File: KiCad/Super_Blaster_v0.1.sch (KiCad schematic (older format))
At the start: 9 parts

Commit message: Started Connections
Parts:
- removed U? (x3): FT601Q, symbol FT601Q
- gave numbers to parts that had none: 1
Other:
- moved on the sheet: U2B, U2C, U2D, U2E
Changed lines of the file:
@@
 EESchema Schematic File Version 2
+LIBS:Super_Blaster_v0.1-rescue
 LIBS:power
 LIBS:device
@@
 LIBS:valves
 LIBS:Homebrew
+LIBS:Super_Blaster_v0.1-cache
 EELAYER 25 0
 EELAYER END
-$Descr A4 11693 8268
+$Descr USLetter 11000 8500
 encoding utf-8
-Sheet 1 1
+Sheet 1 2
 Title ""
 Date ""
@@
 $EndDescr
 $Comp
-L FT601Q U?
-U 1 1 58FB0266
-P 1950 2150
-F 0 "U?" H 1450 3100 60  0000 C CNN
-F 1 "FT601Q" H 1950 1250 60  0000 C CNN
-F 2 "" H 1750 2150 60  0001 C CNN
-F 3 "" H 1750 2150 60  0001 C CNN
-	1    1950 2150
-	1    0    0    -1
-$EndComp
-$Comp
-L FT601Q U?
-U 2 1 58FB02E0
-P 1600 4650
-F 0 "U?" H 1100 5600 60  0000 C CNN
-F 1 "FT601Q" H 1600 3750 60  0000 C CNN
-F 2 "" H 1400 4650 60  0001 C CNN
-F 3 "" H 1400 4650 60  0001 C CNN
-	2    1600 4650
-	1    0    0    -1
-$EndComp
-$Comp
-L FT601Q U?
-U 3 1 58FB0355
-P 1550 6700
-F 0 "U?" H 1050 7650 60  0000 C CNN
-F 1 "FT601Q" H 1550 5800 60  0000 C CNN
-F 2 "" H 1350 6700 60  0001 C CNN
-F 3 "" H 1350 6700 60  0001 C CNN
-	3    1550 6700
-	1    0    0    -1
-$EndComp
-$Comp
-L iCE40-HX8K-CT256 U?
+L iCE40-HX8K-CT256 U2
 U 1 1 58FB0409
 P 3400 1000
-F 0 "U?" H 3600 1250 60  0000 L CNN
+F 0 "U2" H 3600 1250 60  0000 L CNN
 F 1 "iCE40-HX8K-CT256" H 3600 1150 60  0000 L CNN
 F 2 "" H 3400 1000 60  0001 C CNN
@@
 $EndComp
 $Comp
-L iCE40-HX8K-CT256 U?
+L iCE40-HX8K-CT256 U2
 U 2 1 58FB0482
-P 4950 1000
-F 0 "U?" H 5150 1250 60  0000 L CNN
-F 1 "iCE40-HX8K-CT256" H 5150 1150 60  0000 L CNN
-F 2 "" H 4950 1000 60  0001 C CNN
-F 3 "" H 4950 1000 60  0001 C CNN
-	2    4950 1000
+P 4700 1100
+F 0 "U2" H 4900 1350 60  0000 L CNN
+F 1 "iCE40-HX8K-CT256" H 4900 1250 60  0000 L CNN
+F 2 "" H 4700 1100 60  0001 C CNN
+F 3 "" H 4700 1100 60  0001 C CNN
+	2    4700 1100
 	1    0    0    -1
 $EndComp
 $Comp
-L iCE40-HX8K-CT256 U?
+L iCE40-HX8K-CT256 U2
 U 3 1 58FB05E6
-P 6700 1000
-F 0 "U?" H 6900 1250 60  0000 L CNN
-F 1 "iCE40-HX8K-CT256" H 6900 1150 60  0000 L CNN
-F 2 "" H 6700 1000 60  0001 C CNN
-F 3 "" H 6700 1000 60  0001 C CNN
-	3    6700 1000
+P 6100 1200
+F 0 "U2" H 6300 1450 60  0000 L CNN
+F 1 "iCE40-HX8K-CT256" H 6300 1350 60  0000 L CNN
+F 2 "" H 6100 1200 60  0001 C CNN
+F 3 "" H 6100 1200 60  0001 C CNN
+	3    6100 1200
 	1    0    0    -1
 $EndComp
 $Comp
-L iCE40-HX8K-CT256 U?
+L iCE40-HX8K-CT256 U2
 U 4 1 58FB068B
-P 8100 1050
-F 0 "U?" H 8300 1300 60  0000 L CNN
-F 1 "iCE40-HX8K-CT256" H 8300 1200 60  0000 L CNN
-F 2 "" H 8100 1050 60  0001 C CNN
-F 3 "" H 8100 1050 60  0001 C CNN
-	4    8100 1050
+P 7300 1400
+F 0 "U2" H 7500 1650 60  0000 L CNN
+F 1 "iCE40-HX8K-CT256" H 7500 1550 60  0000 L CNN
+F 2 "" H 7300 1400 60  0001 C CNN
+F 3 "" H 7300 1400 60  0001 C CNN
+	4    7300 1400
 	1    0    0    -1
 $EndComp
 $Comp
-L iCE40-HX8K-CT256 U?
+L iCE40-HX8K-CT256 U2
 U 5 1 58FB070B
-P 9650 1000
-F 0 "U?" H 9850 1250 60  0000 L CNN
-F 1 "iCE40-HX8K-CT256" H 9850 1150 60  0000 L CNN
-F 2 "" H 9650 1000 60  0001 C CNN
-F 3 "" H 9650 1000 60  0001 C CNN
-	5    9650 1000
+P 8900 1300
+F 0 "U2" H 9100 1550 60  0000 L CNN
+F 1 "iCE40-HX8K-CT256" H 9100 1450 60  0000 L CNN
+F 2 "" H 8900 1300 60  0001 C CNN
+F 3 "" H 8900 1300 60  0001 C CNN
+	5    8900 1300
 	1    0    0    -1
 $EndComp
 $Comp
-L iCE40-HX8K-CT256 U?
+L iCE40-HX8K-CT256 U2
 U 6 1 58FB07D6
 P 2850 6850
-F 0 "U?" H 3050 7100 60  0000 L CNN
+F 0 "U2" H 3050 7100 60  0000 L CNN
 F 1 "iCE40-HX8K-CT256" H 3050 7000 60  0000 L CNN
 F 2 "" H 2850 6850 60  0001 C CNN
@@
 	1    0    0    -1
 $EndComp
+$Sheet
+S 2200 3400 700  1200
+U 5900EC3E
+F0 "USB_Connection" 60
+F1 "USB_Conn.sch" 60
+F2 "CLK" B R 2900 3700 60
+F3 "DATA16-31" B R 2900 3500 60
+F4 "DATA0-15" B R 2900 3600 60
+$EndSheet
 $EndSCHEMATC

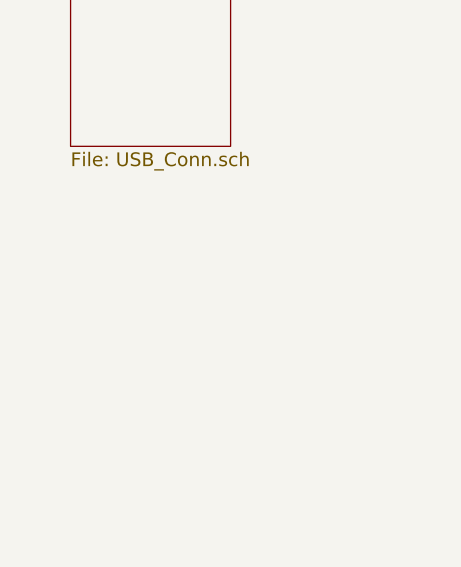
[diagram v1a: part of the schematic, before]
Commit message: added current sense&switch
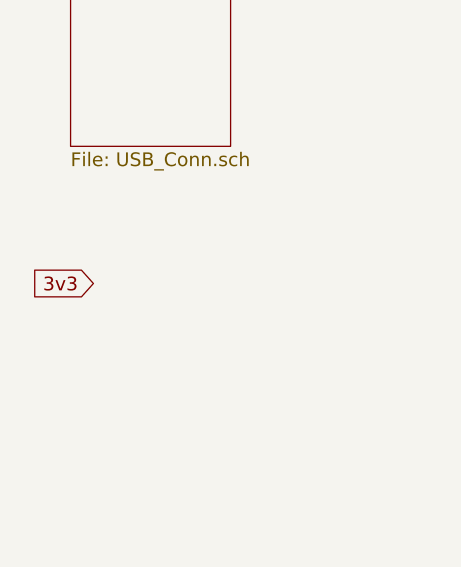
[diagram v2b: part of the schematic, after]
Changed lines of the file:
@@
 F4 "DATA0-15" B R 2900 3600 60
 $EndSheet
+Text GLabel 2300 5200 0    60   Input ~ 0
+3v3
 $EndSCHEMATC

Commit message: more sheets
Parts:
- removed unit 4 of U2
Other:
- moved on the sheet: U2A, U2B, U2C, U2E, U2F
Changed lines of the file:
@@
 $Descr USLetter 11000 8500
 encoding utf-8
-Sheet 1 2
+Sheet 1 3
 Title ""
 Date ""
@@
 L iCE40-HX8K-CT256 U2
 U 1 1 58FB0409
-P 3400 1000
-F 0 "U2" H 3600 1250 60  0000 L CNN
-F 1 "iCE40-HX8K-CT256" H 3600 1150 60  0000 L CNN
-F 2 "" H 3400 1000 60  0001 C CNN
-F 3 "" H 3400 1000 60  0001 C CNN
-	1    3400 1000
+P 4750 1100
+F 0 "U2" H 4950 1350 60  0000 L CNN
+F 1 "iCE40-HX8K-CT256" H 4950 1250 60  0000 L CNN
+F 2 "" H 4750 1100 60  0001 C CNN
+F 3 "" H 4750 1100 60  0001 C CNN
+	1    4750 1100
 	1    0    0    -1
 $EndComp
@@
 L iCE40-HX8K-CT256 U2
 U 2 1 58FB0482
-P 4700 1100
-F 0 "U2" H 4900 1350 60  0000 L CNN
-F 1 "iCE40-HX8K-CT256" H 4900 1250 60  0000 L CNN
-F 2 "" H 4700 1100 60  0001 C CNN
-F 3 "" H 4700 1100 60  0001 C CNN
-	2    4700 1100
+P 7500 1150
+F 0 "U2" H 7700 1400 60  0000 L CNN
+F 1 "iCE40-HX8K-CT256" H 7700 1300 60  0000 L CNN
+F 2 "" H 7500 1150 60  0001 C CNN
+F 3 "" H 7500 1150 60  0001 C CNN
+	2    7500 1150
 	1    0    0    -1
 $EndComp
@@
 L iCE40-HX8K-CT256 U2
 U 3 1 58FB05E6
-P 6100 1200
-F 0 "U2" H 6300 1450 60  0000 L CNN
-F 1 "iCE40-HX8K-CT256" H 6300 1350 60  0000 L CNN
-F 2 "" H 6100 1200 60  0001 C CNN
-F 3 "" H 6100 1200 60  0001 C CNN
-	3    6100 1200
-	1    0    0    -1
-$EndComp
-$Comp
-L iCE40-HX8K-CT256 U2
-U 4 1 58FB068B
-P 7300 1400
-F 0 "U2" H 7500 1650 60  0000 L CNN
-F 1 "iCE40-HX8K-CT256" H 7500 1550 60  0000 L CNN
-F 2 "" H 7300 1400 60  0001 C CNN
-F 3 "" H 7300 1400 60  0001 C CNN
-	4    7300 1400
+P 9000 1150
+F 0 "U2" H 9200 1400 60  0000 L CNN
+F 1 "iCE40-HX8K-CT256" H 9200 1300 60  0000 L CNN
+F 2 "" H 9000 1150 60  0001 C CNN
+F 3 "" H 9000 1150 60  0001 C CNN
+	3    9000 1150
 	1    0    0    -1
 $EndComp
@@
 L iCE40-HX8K-CT256 U2
 U 5 1 58FB070B
-P 8900 1300
-F 0 "U2" H 9100 1550 60  0000 L CNN
-F 1 "iCE40-HX8K-CT256" H 9100 1450 60  0000 L CNN
-F 2 "" H 8900 1300 60  0001 C CNN
-F 3 "" H 8900 1300 60  0001 C CNN
-	5    8900 1300
+P 6050 1200
+F 0 "U2" H 6250 1450 60  0000 L CNN
+F 1 "iCE40-HX8K-CT256" H 6250 1350 60  0000 L CNN
+F 2 "" H 6050 1200 60  0001 C CNN
+F 3 "" H 6050 1200 60  0001 C CNN
+	5    6050 1200
 	1    0    0    -1
 $EndComp
@@
 L iCE40-HX8K-CT256 U2
 U 6 1 58FB07D6
-P 2850 6850
-F 0 "U2" H 3050 7100 60  0000 L CNN
-F 1 "iCE40-HX8K-CT256" H 3050 7000 60  0000 L CNN
-F 2 "" H 2850 6850 60  0001 C CNN
-F 3 "" H 2850 6850 60  0001 C CNN
-	6    2850 6850
+P 2550 1050
+F 0 "U2" H 2750 1300 60  0000 L CNN
+F 1 "iCE40-HX8K-CT256" H 2750 1200 60  0000 L CNN
+F 2 "" H 2550 1050 60  0001 C CNN
+F 3 "" H 2550 1050 60  0001 C CNN
+	6    2550 1050
 	1    0    0    -1
 $EndComp
 $Sheet
-S 2200 3400 700  1200
+S 3500 6650 700  1200
 U 5900EC3E
 F0 "USB_Connection" 60
 F1 "USB_Conn.sch" 60
-F2 "CLK" B R 2900 3700 60
-F3 "DATA16-31" B R 2900 3500 60
-F4 "DATA0-15" B R 2900 3600 60
+F2 "CLK" B R 4200 6950 60
+F3 "DATA16-31" B R 4200 6750 60
+F4 "DATA0-15" B R 4200 6850 60
 $EndSheet
-Text GLabel 2300 5200 0    60   Input ~ 0
+Text GLabel 3950 3300 0    60   Input ~ 0
 3v3
+$Sheet
+S 4850 6650 650  1200
+U 59072317
+F0 "Bottom_Interface" 60
+F1 "Bottom_Interface.sch" 60
+$EndSheet
 $EndSCHEMATC

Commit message: added connections
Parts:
- removed unit 6 of U2
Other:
- moved on the sheet: U2A
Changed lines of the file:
@@
 L iCE40-HX8K-CT256 U2
 U 1 1 58FB0409
-P 4750 1100
-F 0 "U2" H 4950 1350 60  0000 L CNN
-F 1 "iCE40-HX8K-CT256" H 4950 1250 60  0000 L CNN
-F 2 "" H 4750 1100 60  0001 C CNN
-F 3 "" H 4750 1100 60  0001 C CNN
-	1    4750 1100
+P 4550 3500
+F 0 "U2" H 4750 3750 60  0000 L CNN
+F 1 "iCE40-HX8K-CT256" H 4750 3650 60  0000 L CNN
+F 2 "" H 4550 3500 60  0001 C CNN
+F 3 "" H 4550 3500 60  0001 C CNN
+	1    4550 3500
 	1    0    0    -1
 $EndComp
@@
 	1    0    0    -1
 $EndComp
-$Comp
-L iCE40-HX8K-CT256 U2
-U 6 1 58FB07D6
-P 2550 1050
-F 0 "U2" H 2750 1300 60  0000 L CNN
-F 1 "iCE40-HX8K-CT256" H 2750 1200 60  0000 L CNN
-F 2 "" H 2550 1050 60  0001 C CNN
-F 3 "" H 2550 1050 60  0001 C CNN
-	6    2550 1050
-	1    0    0    -1
-$EndComp
 $Sheet
-S 3500 6650 700  1200
+S 3400 5800 700  1700
 U 5900EC3E
 F0 "USB_Connection" 60
 F1 "USB_Conn.sch" 60
-F2 "CLK" B R 4200 6950 60
-F3 "DATA16-31" B R 4200 6750 60
-F4 "DATA0-15" B R 4200 6850 60
+F2 "CLK" B R 4100 6100 60
+F3 "DATA16-31" B R 4100 5900 60
+F4 "DATA0-15" B R 4100 6000 60
+F5 "BE_Array" B R 4100 6200 60
+F6 "~TXE" O R 4100 6300 60
+F7 "~RXF" O R 4100 6400 60
+F8 "~WR" I R 4100 6500 60
+F9 "~RD" I R 4100 6600 60
+F10 "~OE" I R 4100 6700 60
+F11 "~Wakeup" B R 4100 6800 60
+F12 "GPIO0" B R 4100 6900 60
+F13 "GPIO1" B R 4100 7000 60
+F14 "~Reset" I R 4100 7100 60
+F15 "~SIWU" I R 4100 7200 60
+F16 "1.5A_DET" O R 4100 7300 60
+F17 "3A_DET" O R 4100 7400 60
 $EndSheet
-Text GLabel 3950 3300 0    60   Input ~ 0
+Text GLabel 3300 4900 0    60   Input ~ 0
 3v3
 $Sheet
-S 4850 6650 650  1200
+S 4700 5800 700  1700
 U 59072317
 F0 "Bottom_Interface" 60
 F1 "Bottom_Interface.sch" 60
 $EndSheet
+Wire Bus Line
+	4100 5900 4400 5900
 $EndSCHEMATC

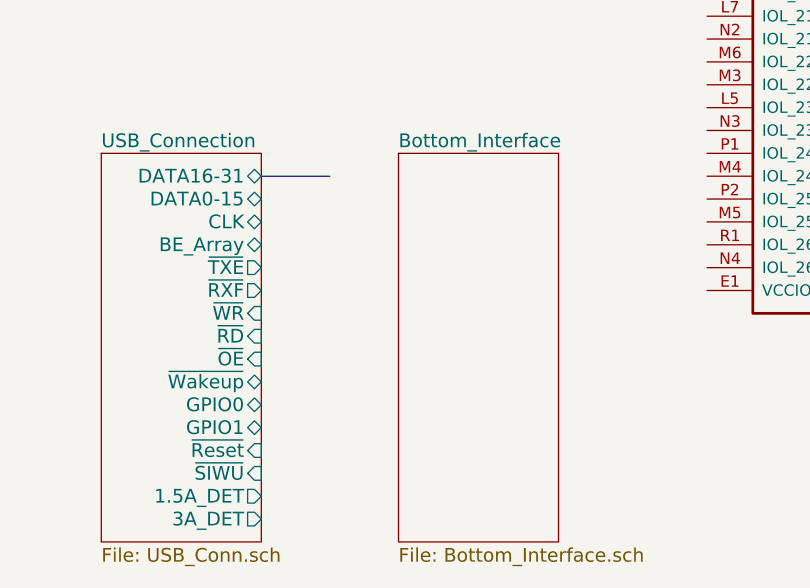
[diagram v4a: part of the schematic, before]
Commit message: working on bottom FPGA
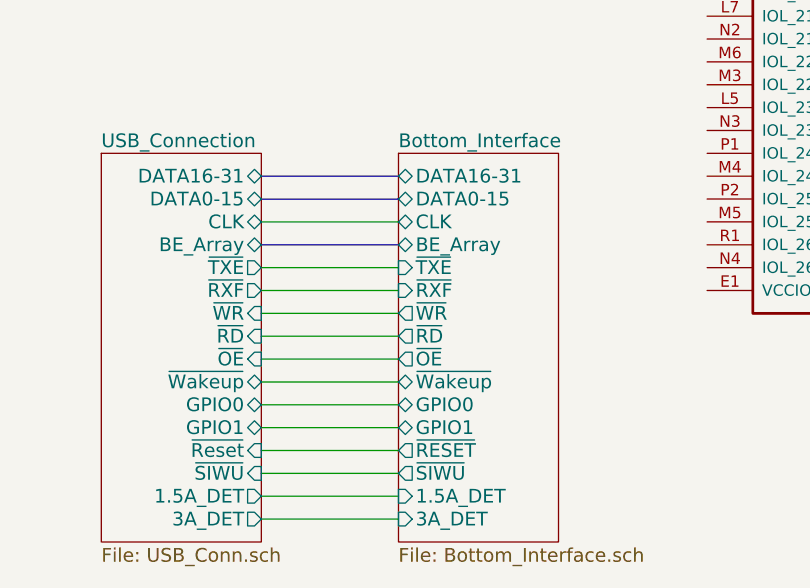
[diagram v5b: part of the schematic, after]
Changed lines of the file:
@@
 F0 "Bottom_Interface" 60
 F1 "Bottom_Interface.sch" 60
+F2 "DATA16-31" B L 4700 5900 60
+F3 "DATA0-15" B L 4700 6000 60
+F4 "CLK" B L 4700 6100 60
+F5 "BE_Array" B L 4700 6200 60
+F6 "~TXE" I L 4700 6300 60
+F7 "~RXF" I L 4700 6400 60
+F8 "~WR" O L 4700 6500 60
+F9 "~RD" O L 4700 6600 60
+F10 "~OE" O L 4700 6700 60
+F11 "~Wakeup" B L 4700 6800 60
+F12 "GPIO0" B L 4700 6900 60
+F13 "GPIO1" B L 4700 7000 60
+F14 "~RESET" O L 4700 7100 60
+F15 "~SIWU" O L 4700 7200 60
+F16 "1.5A_DET" I L 4700 7300 60
+F17 "3A_DET" I L 4700 7400 60
 $EndSheet
 Wire Bus Line
-	4100 5900 4400 5900
+	4100 5900 4700 5900
+Wire Bus Line
+	4100 6000 4700 6000
+Wire Bus Line
+	4100 6200 4700 6200
+Wire Wire Line
+	4100 6100 4700 6100
+Wire Wire Line
+	4100 6300 4700 6300
+Wire Wire Line
+	4100 6400 4700 6400
+Wire Wire Line
+	4700 6500 4100 6500
+Wire Wire Line
+	4100 6600 4700 6600
+Wire Wire Line
+	4700 6700 4100 6700
+Wire Wire Line
+	4100 6800 4700 6800
+Wire Wire Line
+	4100 6900 4700 6900
+Wire Wire Line
+	4100 7000 4700 7000
+Wire Wire Line
+	4100 7100 4700 7100
+Wire Wire Line
+	4100 7200 4700 7200
+Wire Wire Line
+	4100 7300 4700 7300
+Wire Wire Line
+	4100 7400 4700 7400
 $EndSCHEMATC

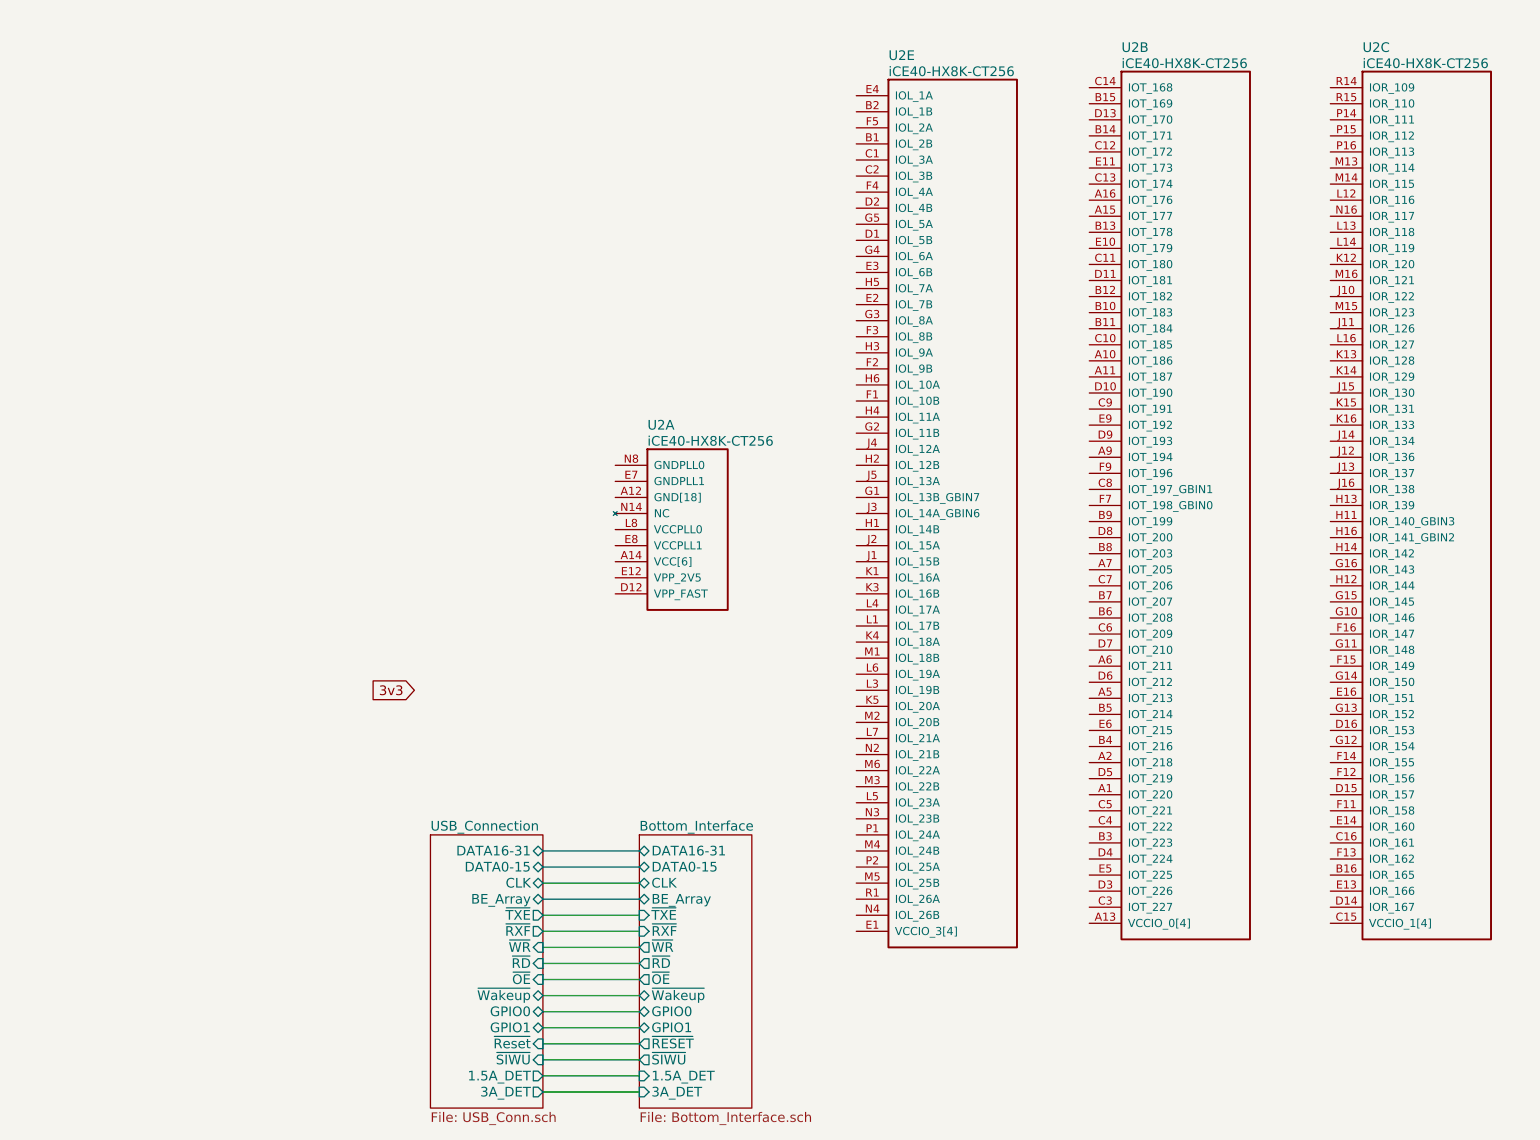
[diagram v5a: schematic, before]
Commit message: fix bus route
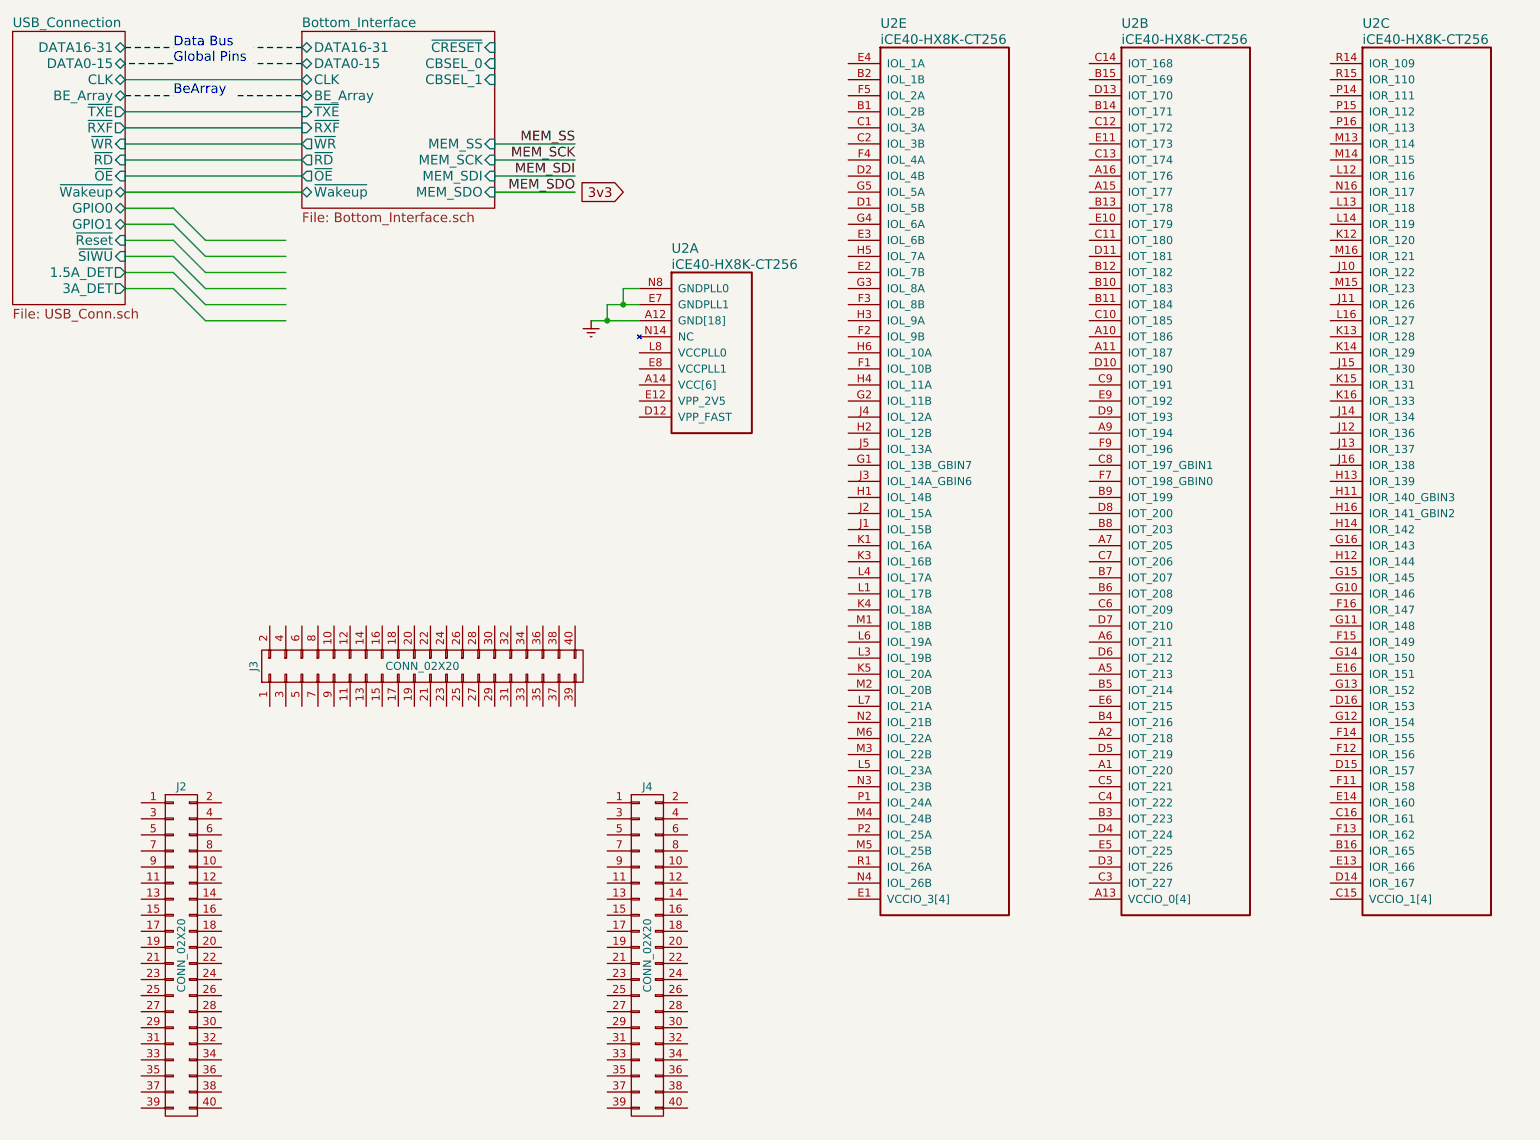
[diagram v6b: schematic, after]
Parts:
- added J2, J3, J4: CONN_02X20, Pin_Headers:Pin_Header_Straight_2x20_Pitch1.27mm, symbol CONN_02X20
- U2: footprint (none) -> Homebrew:caBGA_256_.8p_14x14mm
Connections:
- net labels added: Earth, MEM_SCK, MEM_SDI, MEM_SDO, MEM_SS
- wire segments 13 -> 34
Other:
- note added: "BeArray"
- note added: "Data Bus \nGlobal Pins"
- moved on the sheet: U2A, U2B, U2C, U2E
